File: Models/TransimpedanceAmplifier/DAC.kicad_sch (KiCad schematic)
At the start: 6 parts, among them U2 DAC81401PWR

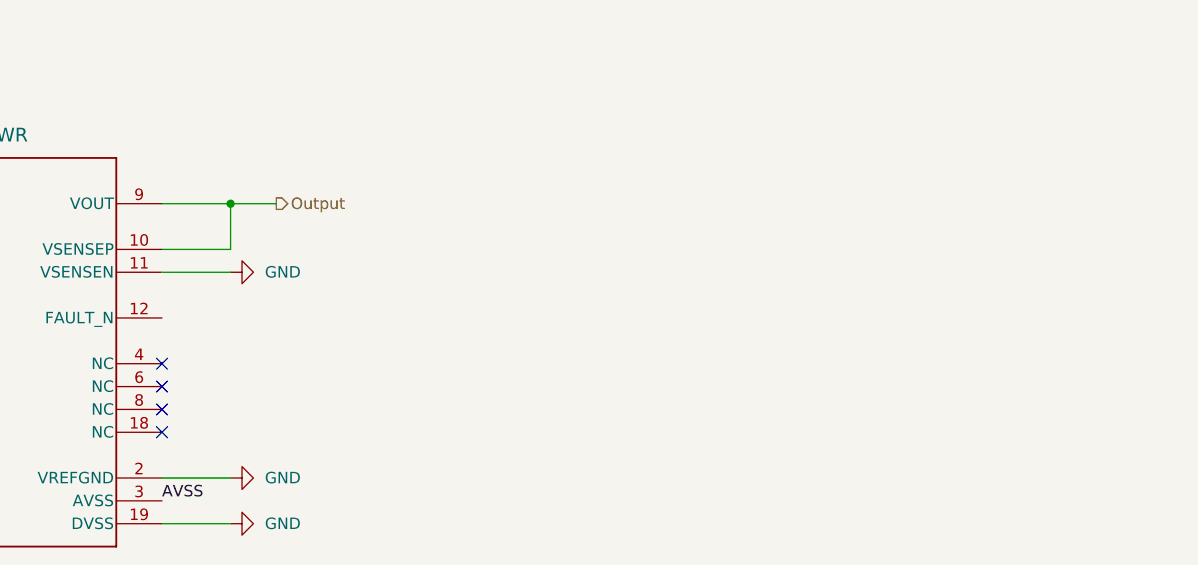
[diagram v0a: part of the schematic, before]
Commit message: Resolved an unknown about the unconnected DAC FAULT pin
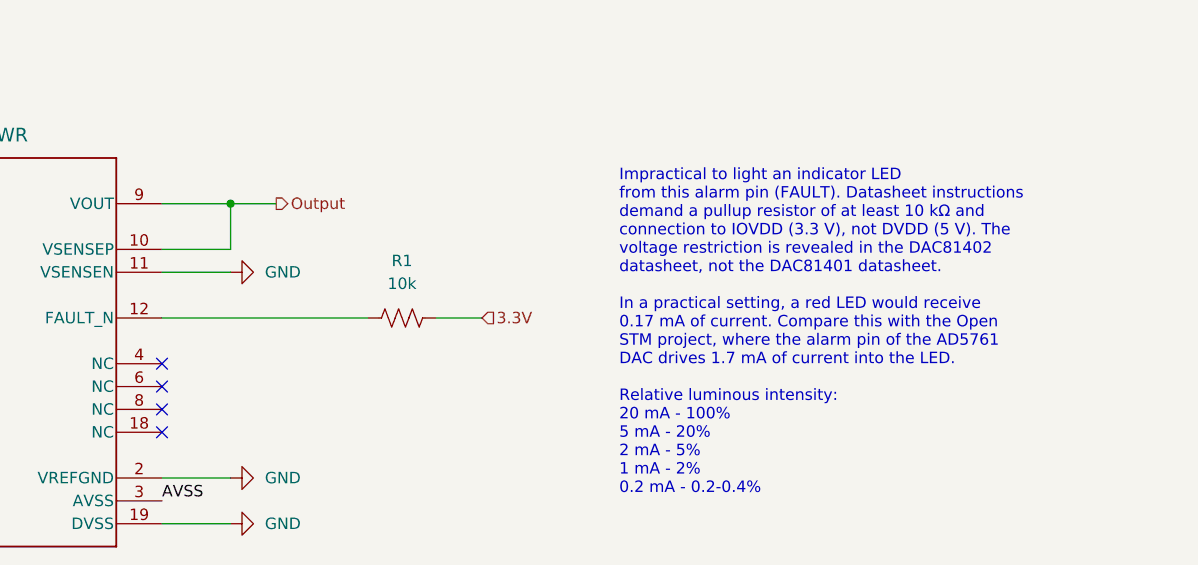
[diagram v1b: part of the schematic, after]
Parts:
- added R1: 10k, symbol Device:R_US
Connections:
- net 3.3V: now also R1.2
- net at U2.12 (FAULT_N): now also R1.1
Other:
- note added: "Impractical to light an indicator LED from this alarm pin (FAULT). Datasheet instructions demand a pullup resistor of at least 10 kΩ and connection to IOVDD (3.3 V), not DVDD (5 V). The voltage restriction is revealed in the DAC81402 datasheet, not the DAC81401 datasheet. In a practical setting, a red LED would receive 0.17 mA of current. Compare this with the Open STM project, where the alarm pi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"
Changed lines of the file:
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@@
 	(generator_version "9.0")
 	(paper "A4")
+	(text "Impractical to light an indicator LED\nfrom this alarm pin (FAULT). Datasheet instructions\ndemand a pullup resistor of at least 10 kΩ and\nconnection to IOVDD (3.3 V), not DVDD (5 V). The\nvoltage restriction is revealed in the DAC81402\ndatasheet, not the DAC81401 datasheet.\n\nIn a practical setting, a red LED would receive\n0.17 mA of current. Compare this with the Open\nSTM project, where the alarm pin of the AD5761\nDAC drives 1.7 mA of current into the LED.\n\nRelative luminous intensity:\n20 mA - 100%\n5 mA - 20%\n2 mA - 5%\n1 mA - 2%\n0.2 mA - 0.2-0.4%"
+		(exclude_from_sim no)
+		(at 167.64 102.87 0)
+		(effects
+			(font
+				(size 1.27 1.27)
+			)
+			(justify left top)
+		)
+	)
 	(junction
 		(at 48.26 38.1)
@@
 	(wire
 		(pts
+			(xy 116.84 119.38) (xy 139.7 119.38)
+		)
+		(stroke
+			(width 0)
+			(type default)
+		)
+	)
+	(wire
+		(pts
 			(xy 40.64 55.88) (xy 40.64 58.42)
 		)
@@
 		(pts
 			(xy 48.26 73.66) (xy 53.34 73.66)
+		)
+		(stroke
+			(width 0)
+			(type default)
+		)
+	)
+	(wire
+		(pts
+			(xy 147.32 119.38) (xy 152.4 119.38)
 		)
 		(stroke
@@
 			)
 			(justify right)
+		)
+	)
+	(hierarchical_label "3.3V"
+		(shape input)
+		(at 152.4 119.38 0)
+		(effects
+			(font
+				(size 1.27 1.27)
+			)
+			(justify left)
 		)
 	)
@@
 					(unit 1)
 				)
+			)
+		)
+	)
+	(symbol
+		(lib_id "Device:R_US")
+		(at 143.51 119.38 90)
+		(unit 1)
+		(exclude_from_sim no)
+		(in_bom yes)
+		(on_board yes)
+		(dnp no)
+		(fields_autoplaced yes)
+		(property "Reference" "R1"
+			(at 143.51 113.03 90)
+			(effects
+				(font
+					(size 1.27 1.27)
+				)
+			)
+		)
+		(property "Value" "10k"
+			(at 143.51 115.57 90)
+			(effects
+				(font
+					(size 1.27 1.27)
+				)
+			)
+		)
+		(property "Footprint" ""
+			(at 143.764 118.364 90)
+			(effects
+				(font
+					(size 1.27 1.27)
+				)
+				(hide yes)
+			)
+		)
+		(property "Datasheet" "~"
+			(at 143.51 119.38 0)
+			(effects
+				(font
+					(size 1.27 1.27)
+				)
+				(hide yes)
+			)
+		)
+		(property "Description" "Resistor, US symbol"
+			(at 143.51 119.38 0)
+			(effects
+				(font
+					(size 1.27 1.27)
+				)
+				(hide yes)
+			)
+		)
+		(pin "1"
+		)
+		(pin "2"
+		)
+		(instances
+			(project ""
+				(path "/ec9f2ae3-e40d-40eb-9760-2b611ee8efd1/7e303428-a18c-4ad4-b002-5ab9c6631588/77c98efe-b6d0-43b4-bfa9-b392bfbf9a85"
+					(reference "R1")
+					(unit 1)
+				)

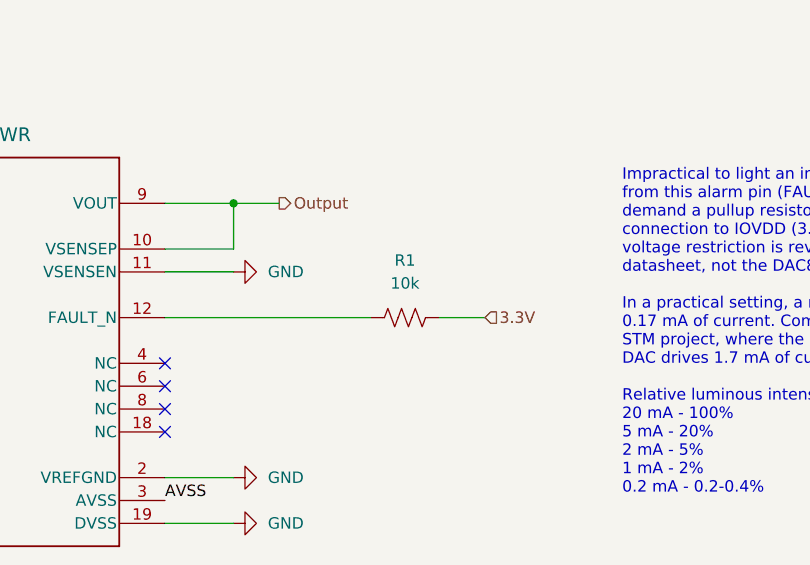
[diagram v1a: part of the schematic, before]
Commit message: Connected all pins of the data converters
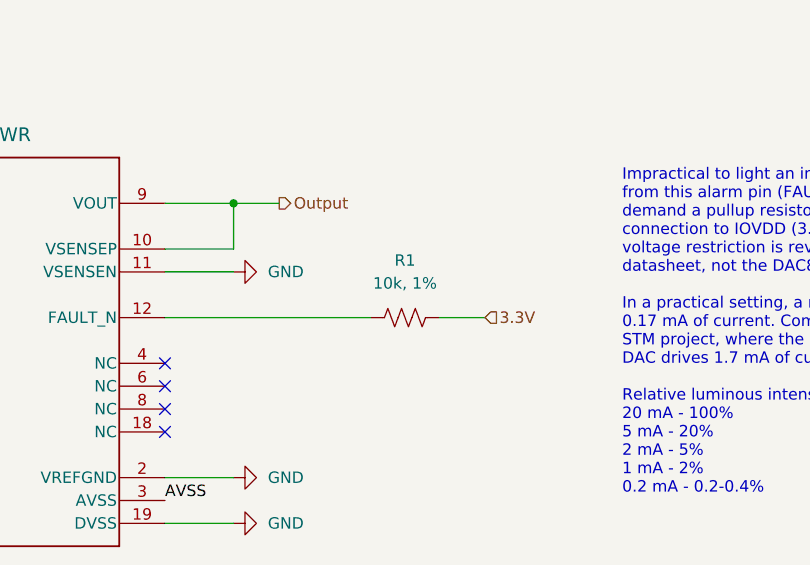
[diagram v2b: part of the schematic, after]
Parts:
- R1: value 10k -> 10k, 1%; Purchase Link (none) -> https://www.digikey.com/en/products/detail/vishay-dale/CRCW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
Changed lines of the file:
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@@
 			)
 		)
-		(property "Value" "10k"
+		(property "Value" "10k, 1%"
 			(at 143.51 115.57 90)
 			(effects
@@
 			(at 143.51 119.38 0)
 			(effects
+				(font
+					(size 1.27 1.27)
+				)
+				(hide yes)
+			)
+		)
+		(property "Purchase Link" "https://www.digikey.com/en/products/detail/vishay-dale/CRCW060310K0FKEA/1174782"
+			(at 143.51 119.38 0)
+			(effects

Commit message: Save progress
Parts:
- U2: footprint PW0020A-IPC_A -> (none)
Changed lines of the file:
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@@
 			)
 		)
-		(property "Footprint" "PW0020A-IPC_A"
+		(property "Footprint" ""
 			(at 72.39 106.68 0)
 			(effects

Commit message: Save progress
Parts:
- U2: value DAC81401PWR -> DAC81401
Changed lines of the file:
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@@
 			)
 		)
-		(property "Value" "DAC81401PWR"
+		(property "Value" "DAC81401"
 			(at 93.98 99.06 0)
 			(effects

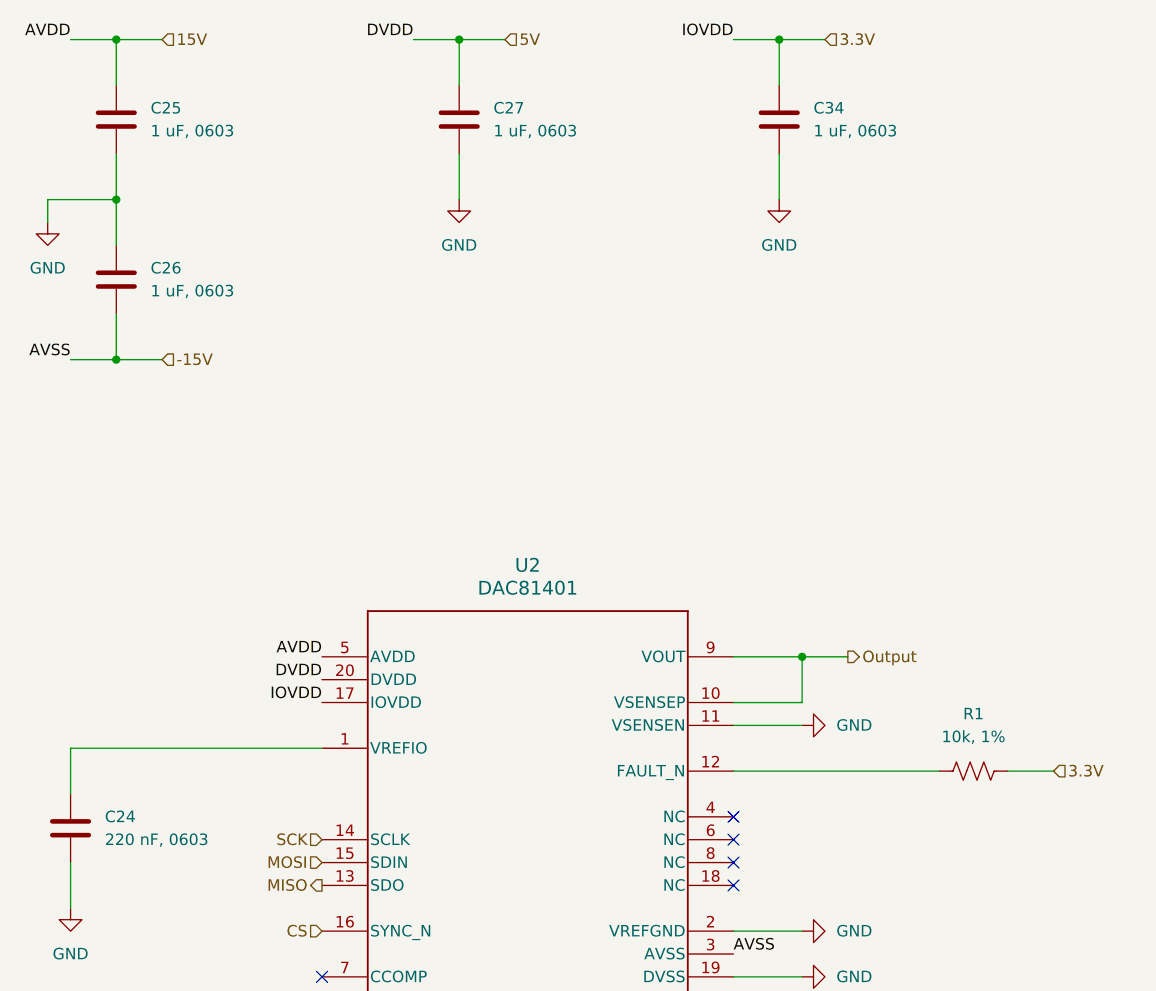
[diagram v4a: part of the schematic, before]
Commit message: Overhauled all of the annotations
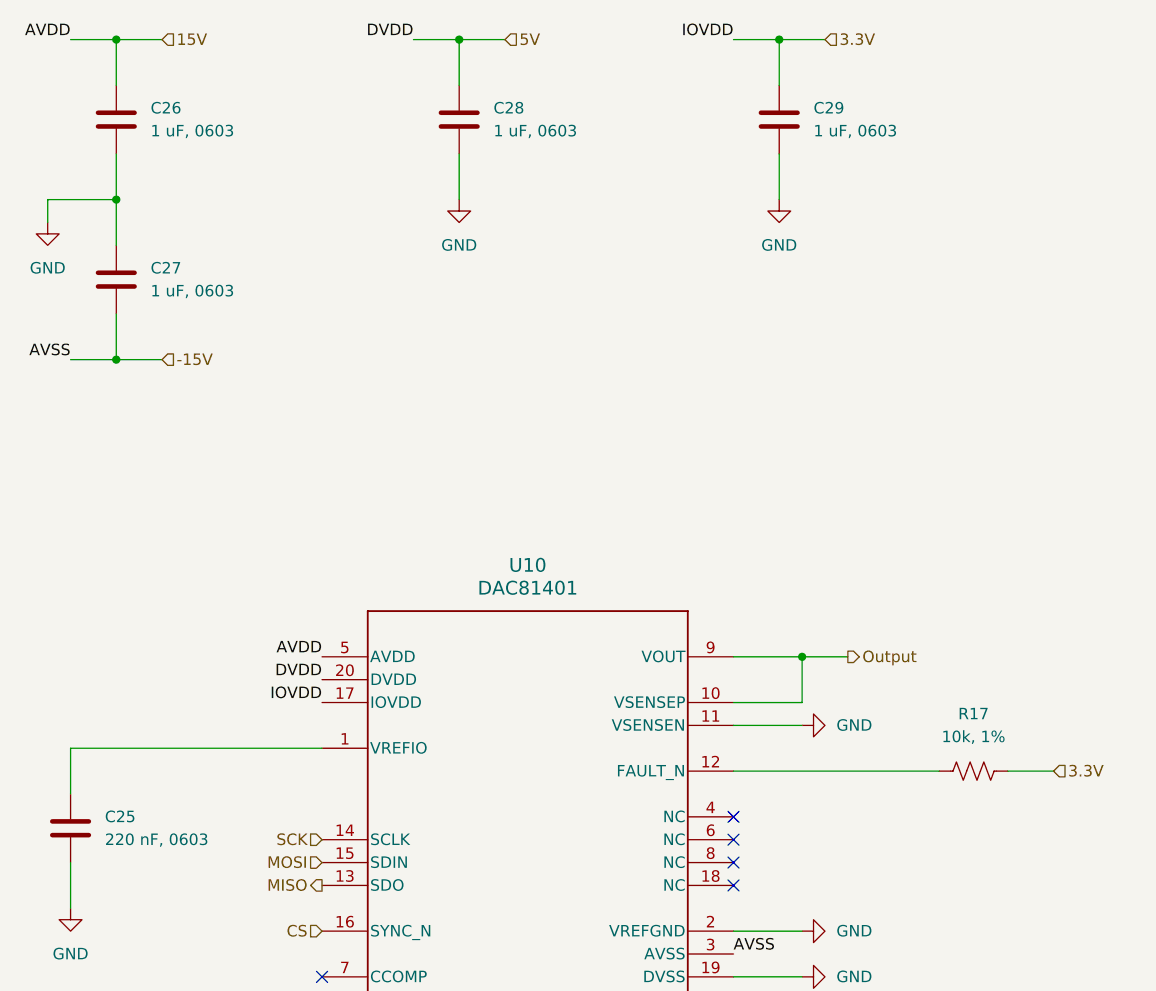
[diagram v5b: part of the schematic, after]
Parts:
- renumbered C24 to C25, C25 to C26, C26 to C27, C27 to C28, C34 to C29, R1 to R17, U2 to U10
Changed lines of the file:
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@@
 		(dnp no)
 		(fields_autoplaced yes)
-		(property "Reference" "#PWR031"
+		(property "Reference" "#PWR039"
 			(at 43.18 140.97 0)
 			(effects
@@
 			(project ""
 				(path "/ec9f2ae3-e40d-40eb-9760-2b611ee8efd1/7e303428-a18c-4ad4-b002-5ab9c6631588/77c98efe-b6d0-43b4-bfa9-b392bfbf9a85"
-					(reference "#PWR031")
+					(reference "#PWR039")
 					(unit 1)
 				)
@@
 		(dnp no)
 		(fields_autoplaced yes)
-		(property "Reference" "#PWR07"
+		(property "Reference" "#PWR044"
 			(at 130.81 142.24 0)
 			(effects
@@
 			(project ""
 				(path "/ec9f2ae3-e40d-40eb-9760-2b611ee8efd1/7e303428-a18c-4ad4-b002-5ab9c6631588/77c98efe-b6d0-43b4-bfa9-b392bfbf9a85"
-					(reference "#PWR07")
+					(reference "#PWR044")
 					(unit 1)
 				)
@@
 		(dnp no)
 		(fields_autoplaced yes)
-		(property "Reference" "#PWR08"
+		(property "Reference" "#PWR043"
 			(at 130.81 137.16 0)
 			(effects
@@
 			(project "TransimpedanceAmplifier"
 				(path "/ec9f2ae3-e40d-40eb-9760-2b611ee8efd1/7e303428-a18c-4ad4-b002-5ab9c6631588/77c98efe-b6d0-43b4-bfa9-b392bfbf9a85"
-					(reference "#PWR08")
+					(reference "#PWR043")
 					(unit 1)
 				)
@@
 		(dnp no)
 		(fields_autoplaced yes)
-		(property "Reference" "#PWR033"
+		(property "Reference" "#PWR038"
 			(at 40.64 64.77 0)
 			(effects
@@
 			(project ""
 				(path "/ec9f2ae3-e40d-40eb-9760-2b611ee8efd1/7e303428-a18c-4ad4-b002-5ab9c6631588/77c98efe-b6d0-43b4-bfa9-b392bfbf9a85"
-					(reference "#PWR033")
+					(reference "#PWR038")
 					(unit 1)
 				)
@@
 		(dnp no)
 		(fields_autoplaced yes)
-		(property "Reference" "#PWR032"
+		(property "Reference" "#PWR042"
 			(at 130.81 114.3 0)
 			(effects
@@
 			(project "TransimpedanceAmplifier"
 				(path "/ec9f2ae3-e40d-40eb-9760-2b611ee8efd1/7e303428-a18c-4ad4-b002-5ab9c6631588/77c98efe-b6d0-43b4-bfa9-b392bfbf9a85"
-					(reference "#PWR032")
+					(reference "#PWR042")
 					(unit 1)
 				)
@@
 		(dnp no)
 		(fields_autoplaced yes)
-		(property "Reference" "#PWR046"
+		(property "Reference" "#PWR041"
 			(at 121.92 62.23 0)
 			(effects
@@
 			(project "TransimpedanceAmplifier"
 				(path "/ec9f2ae3-e40d-40eb-9760-2b611ee8efd1/7e303428-a18c-4ad4-b002-5ab9c6631588/77c98efe-b6d0-43b4-bfa9-b392bfbf9a85"
-					(reference "#PWR046")
+					(reference "#PWR041")
 					(unit 1)
 				)
@@
 		(dnp no)
 		(fields_autoplaced yes)
-		(property "Reference" "C25"
+		(property "Reference" "C26"
 			(at 52.07 45.7199 0)
 			(effects
@@
 			(project ""
 				(path "/ec9f2ae3-e40d-40eb-9760-2b611ee8efd1/7e303428-a18c-4ad4-b002-5ab9c6631588/77c98efe-b6d0-43b4-bfa9-b392bfbf9a85"
-					(reference "C25")
+					(reference "C26")
 					(unit 1)
 				)
@@
 		(dnp no)
 		(fields_autoplaced yes)
-		(property "Reference" "C34"
+		(property "Reference" "C29"
 			(at 125.73 45.7199 0)
 			(effects
@@
 			(project "TransimpedanceAmplifier"
 				(path "/ec9f2ae3-e40d-40eb-9760-2b611ee8efd1/7e303428-a18c-4ad4-b002-5ab9c6631588/77c98efe-b6d0-43b4-bfa9-b392bfbf9a85"
-					(reference "C34")
+					(reference "C29")
 					(unit 1)
 				)
@@
 		(dnp no)
 		(fields_autoplaced yes)
-		(property "Reference" "#PWR035"
+		(property "Reference" "#PWR040"
 			(at 86.36 62.23 0)
 			(effects
@@
 			(project ""
 				(path "/ec9f2ae3-e40d-40eb-9760-2b611ee8efd1/7e303428-a18c-4ad4-b002-5ab9c6631588/77c98efe-b6d0-43b4-bfa9-b392bfbf9a85"
-					(reference "#PWR035")
+					(reference "#PWR040")
 					(unit 1)
 				)
@@
 		(dnp no)
 		(fields_autoplaced yes)
-		(property "Reference" "C27"
+		(property "Reference" "C28"
 			(at 90.17 45.7199 0)
 			(effects
@@
 			(project "TransimpedanceAmplifier"
 				(path "/ec9f2ae3-e40d-40eb-9760-2b611ee8efd1/7e303428-a18c-4ad4-b002-5ab9c6631588/77c98efe-b6d0-43b4-bfa9-b392bfbf9a85"
-					(reference "C27")
+					(reference "C28")
 					(unit 1)
 				)
@@
 		(dnp no)
 		(fields_autoplaced yes)
-		(property "Reference" "R1"
+		(property "Reference" "R17"
 			(at 143.51 113.03 90)
 			(effects
@@
 			(project ""
 				(path "/ec9f2ae3-e40d-40eb-9760-2b611ee8efd1/7e303428-a18c-4ad4-b002-5ab9c6631588/77c98efe-b6d0-43b4-bfa9-b392bfbf9a85"
-					(reference "R1")
+					(reference "R17")
 					(unit 1)
 				)
@@
 		(dnp no)
 		(fields_autoplaced yes)
-		(property "Reference" "C24"
+		(property "Reference" "C25"
 			(at 46.99 124.4599 0)
 			(effects
@@
 			(project ""
 				(path "/ec9f2ae3-e40d-40eb-9760-2b611ee8efd1/7e303428-a18c-4ad4-b002-5ab9c6631588/77c98efe-b6d0-43b4-bfa9-b392bfbf9a85"
-					(reference "C24")
+					(reference "C25")
 					(unit 1)
 				)
@@
 		(dnp no)
 		(fields_autoplaced yes)
-		(property "Reference" "U2"
+		(property "Reference" "U10"
 			(at 93.98 96.52 0)
 			(effects
@@
 			(project ""
 				(path "/ec9f2ae3-e40d-40eb-9760-2b611ee8efd1/7e303428-a18c-4ad4-b002-5ab9c6631588/77c98efe-b6d0-43b4-bfa9-b392bfbf9a85"
-					(reference "U2")
+					(reference "U10")
 					(unit 1)
 				)
@@
 		(dnp no)
 		(fields_autoplaced yes)
-		(property "Reference" "C26"
+		(property "Reference" "C27"
 			(at 52.07 63.4999 0)
 			(effects
@@
 			(project "TransimpedanceAmplifier"
 				(path "/ec9f2ae3-e40d-40eb-9760-2b611ee8efd1/7e303428-a18c-4ad4-b002-5ab9c6631588/77c98efe-b6d0-43b4-bfa9-b392bfbf9a85"
-					(reference "C26")
-					(unit 1)
-				)
+					(reference "C27")
+					(unit 1)
+				)
